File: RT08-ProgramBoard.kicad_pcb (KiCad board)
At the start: 2 copper layers, 325 parts, among them J1 PWR/Addr, J2 Inst-1, J3 Inst-2, J4 Data-1, J5 Data-2

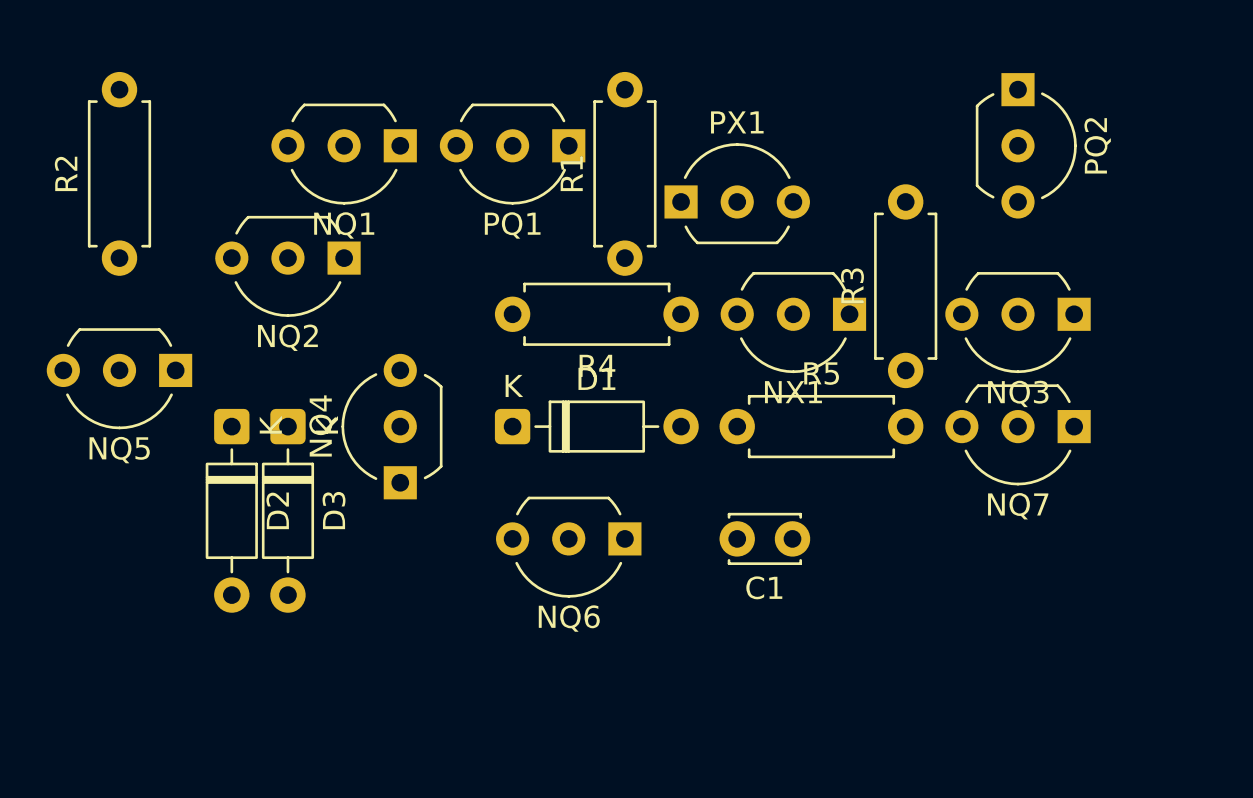
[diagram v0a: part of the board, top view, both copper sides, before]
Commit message: Designing new register circuit
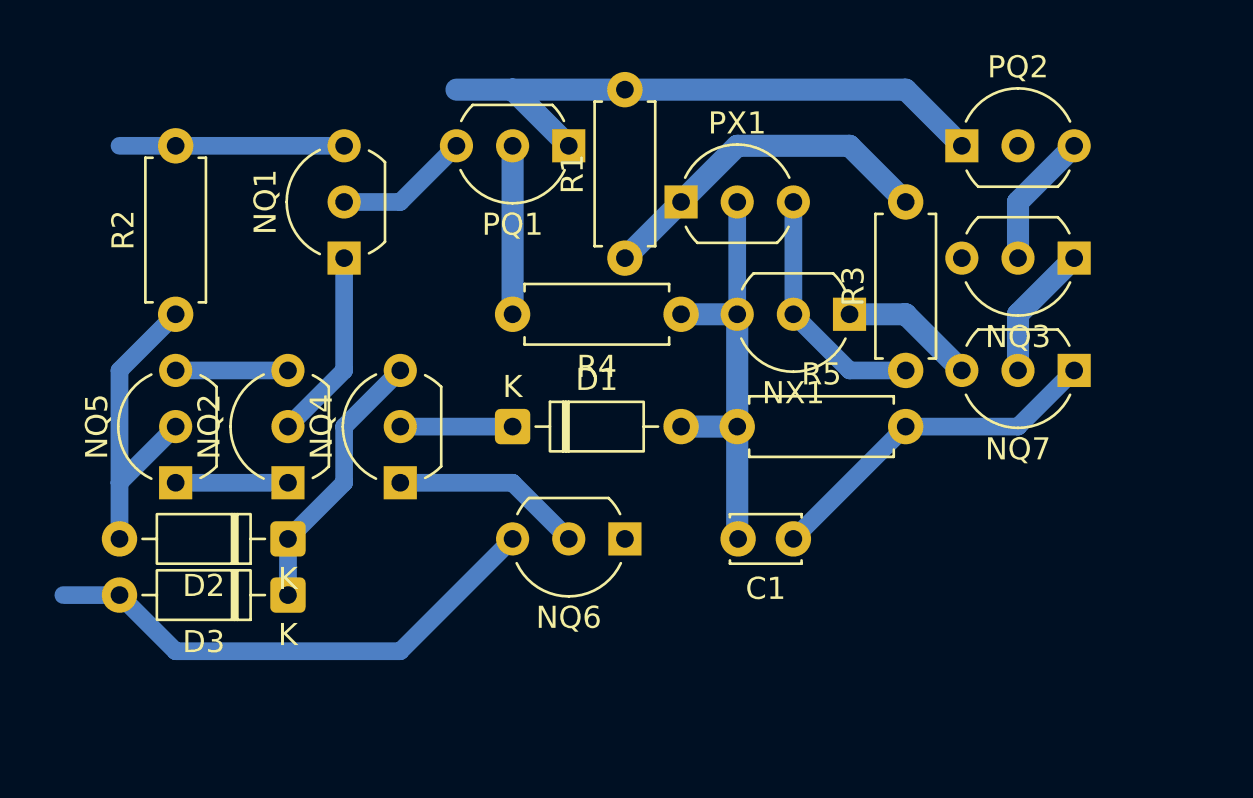
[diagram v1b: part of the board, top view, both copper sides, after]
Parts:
- moved NQ2 10.5 mm to (71.1, 45.7), turned to 90 degrees
- moved D3 7.62 mm to (71.1, 50.8), turned to 180 degrees
- moved NQ1 5.68 mm to (73.7, 35.6), turned to 90 degrees
- moved D2 5.68 mm to (71.1, 48.3), turned to 180 degrees
- moved NQ5 5.08 mm to (66.0, 45.7), turned to 90 degrees
- moved PQ2 3.59 mm to (101.6, 30.5), turned to 0 degrees
- moved R2 3.59 mm to (66.0, 38.1)
- moved NQ3 2.54 mm to (106.7, 35.6)
- moved NQ7 2.54 mm to (106.7, 40.6)
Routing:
- net +5V: track 0.00 -> 27.5 mm
- net /Rst: track 0.00 -> 23.5 mm
- net GND: track 0.00 -> 20.9 mm
- net Net-(D1-A): track 0.00 -> 20.3 mm
- net Net-(PX1-E): track 0.00 -> 15.9 mm
- net Net-(D2-A): track 0.00 -> 14.8 mm
- net Net-(D2-K): track 0.00 -> 12.3 mm
- net Net-(NX1-C): track 0.00 -> 11.2 mm
- net /WEn: track 0.00 -> 10.2 mm
- net Net-(NQ4-E): track 0.00 -> 8.67 mm
- net Net-(NQ1-E): track 0.00 -> 8.67 mm
- net Net-(PQ1-C): track 0.00 -> 7.62 mm
- net Net-(NQ3-C): track 0.00 -> 6.13 mm
- net Net-(NQ3-E): track 0.00 -> 6.13 mm
- net Net-(NQ1-C): track 0.00 -> 6.13 mm
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
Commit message: New design completed
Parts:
- removed D33, D34, D35, D36, D37, D38, D39, D40, D41, D42, D43, D44, D45, D46, D47, D48: 30V0.2A, Diode_THT:D_DO-35_SOD27_P7.62mm_Horizontal
- removed NQ100, NQ101, NQ103, NQ105, NQ106, NQ107, NQ108, NQ110, NQ112, NQ98, NQ99: DTC114E-THT, Package_TO_SOT_THT:TO-92_Inline_Wide
- removed NQ102, NQ104, NQ109, NQ111, NQ97: DTC143E-THT, Package_TO_SOT_THT:TO-92_Inline_Wide
- J1: value PWR/Addr -> PWR/Ctrl
- NQ10, NQ16, NQ22, NQ28, NQ40, NQ52, NQ58, NQ64, NQ70, NQ82, NQ94: value DTC114E-THT -> DTC143E-THT
- NQ11, NQ13, NQ18, NQ20, NQ25, NQ27, NQ32, NQ39, NQ41, NQ48, NQ53, NQ55, NQ6, NQ60, NQ62, NQ67, NQ69, NQ74, NQ81, NQ83, NQ90, NQ95: value DTC143E-THT -> DTC114E-THT
- moved J1 322.0 mm to (55.9, 137.2), turned to -90 degrees
- moved PQ25 315.1 mm to (53.3, 109.2), turned to 180 degrees
- moved C13 310.3 mm to (55.9, 119.4)
- moved R61 310.1 mm to (38.1, 116.8), turned to 90 degrees
- moved PX13 309.7 mm to (58.4, 111.8)
- moved J2 308.9 mm to (73.7, 137.2), turned to -90 degrees
- moved NQ51 305.3 mm to (40.6, 99.1), turned to 90 degrees
- moved NQ50 297.7 mm to (48.3, 91.4), turned to 180 degrees
- moved NX13 296.4 mm to (66.0, 116.8), turned to 180 degrees
- moved J3 295.7 mm to (91.4, 137.2), turned to -90 degrees
- moved R62 291.6 mm to (55.9, 114.3), turned to 90 degrees
- moved NQ52 290.5 mm to (66.0, 96.5), turned to 180 degrees
- moved R64 288.5 mm to (58.4, 116.8), turned to 180 degrees
- moved NQ27 287.9 mm to (40.6, 71.1), turned to 90 degrees
- moved PQ26 285.8 mm to (71.1, 109.2)
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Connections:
- C1 pad 2: Net-(D1-A) -> Net-(NQ4-C)
- C10 pad 2: Net-(D28-A) -> Net-(NQ58-C)
- C11 pad 2: Net-(D31-A) -> Net-(NQ64-C)
- C12 pad 2: Net-(D34-A) -> Net-(NQ70-C)
- C13 pad 2: Net-(D37-A) -> Net-(NQ76-C)
- C14 pad 2: Net-(D40-A) -> Net-(NQ82-C)
- C15 pad 2: Net-(D43-A) -> Net-(NQ88-C)
- C16 pad 2: Net-(D46-A) -> Net-(NQ94-C)
- C2 pad 2: Net-(D4-A) -> Net-(NQ10-C)
- C3 pad 2: Net-(D7-A) -> Net-(NQ16-C)
- C4 pad 2: Net-(D10-A) -> Net-(NQ22-C)
- C5 pad 2: Net-(D13-A) -> Net-(NQ28-C)
- C6 pad 2: Net-(D16-A) -> Net-(NQ34-C)
- C7 pad 2: Net-(D19-A) -> Net-(NQ40-C)
- C8 pad 2: Net-(D22-A) -> Net-(NQ46-C)
- C9 pad 2: Net-(D25-A) -> Net-(NQ52-C)
- D10 pad 2: Net-(D10-A) -> /Rst
- D14 pad 1: Net-(D14-K) -> Net-(D13-K)
- D14 pad 2: Net-(D14-A) -> /Rst
- D15 pad 1: Net-(D14-K) -> Net-(D15-K)
- D15 pad 2: /Rst -> Net-(D15-A)
- D16 pad 1: Net-(D16-K) -> Net-(D15-K)
- D16 pad 2: Net-(D16-A) -> /Rst
- D2 pad 1: Net-(D2-K) -> Net-(D1-K)
- D2 pad 2: Net-(D2-A) -> /Rst
- D20 pad 1: Net-(D20-K) -> Net-(D19-K)
- D20 pad 2: Net-(D20-A) -> /Rst
- D21 pad 1: Net-(D20-K) -> Net-(D21-K)
- D21 pad 2: /Rst -> Net-(D21-A)
- D22 pad 1: Net-(D22-K) -> Net-(D21-K)
- D22 pad 2: Net-(D22-A) -> /Rst
- D26 pad 1: Net-(D26-K) -> Net-(D25-K)
- D26 pad 2: Net-(D26-A) -> /Rst
- D27 pad 1: Net-(D26-K) -> Net-(D27-K)
- D27 pad 2: /Rst -> Net-(D27-A)
- D28 pad 1: Net-(D28-K) -> Net-(D27-K)
- D28 pad 2: Net-(D28-A) -> /Rst
- D3 pad 1: Net-(D2-K) -> Net-(D3-K)
- D3 pad 2: /Rst -> Net-(D3-A)
- D32 pad 1: Net-(D32-K) -> Net-(D31-K)
- D32 pad 2: Net-(D32-A) -> /Rst
- D4 pad 1: Net-(D4-K) -> Net-(D3-K)
- D4 pad 2: Net-(D4-A) -> /Rst
- D8 pad 1: Net-(D8-K) -> Net-(D7-K)
- D8 pad 2: Net-(D8-A) -> /Rst
- D9 pad 1: Net-(D8-K) -> Net-(D10-K)
- D9 pad 2: /Rst -> Net-(D9-A)
- J1 pad 2: /WEn -> /DEn
- J1 pad 3: /DEn -> /WEn
- NQ10 pad 1: Net-(NQ10-E) -> GND
- NQ10 pad 3: /DEn -> Net-(D3-K)
- NQ11 pad 2: Net-(D4-K) -> Net-(NQ11-C)
- NQ11 pad 3: Net-(D5-K) -> /DEn
- NQ12 pad 2: Net-(D5-A) -> Net-(NQ11-E)
- NQ12 pad 3: /D1 -> Net-(NQ12-B)
- NQ13 pad 1: GND -> Net-(NQ13-E)
- NQ13 pad 2: Net-(NQ11-E) -> Net-(NQ13-C)
- NQ13 pad 3: /Rst -> /WEn
- NQ14 pad 2: Net-(NQ10-E) -> Net-(NQ13-E)
- NQ14 pad 3: Net-(NQ14-B) -> /D2
- NQ15 pad 1: Net-(NQ15-E) -> GND
- NQ15 pad 2: Net-(NQ15-C) -> Net-(D5-A)
- NQ15 pad 3: /WEn -> /D2
- NQ16 pad 2: Net-(NQ15-E) -> Net-(NQ16-C)
- NQ16 pad 3: /D2 -> Net-(D5-K)
- NQ18 pad 1: Net-(NQ18-E) -> GND
- NQ18 pad 2: Net-(D7-K) -> Net-(NQ17-E)
- NQ18 pad 3: Net-(D8-K) -> Net-(NQ18-B)
- NQ19 pad 1: GND -> Net-(NQ19-E)
- NQ19 pad 2: Net-(D8-A) -> Net-(NQ19-C)
- NQ19 pad 3: /D2 -> /WEn
- NQ20 pad 2: Net-(NQ18-E) -> Net-(NQ19-E)
- NQ20 pad 3: /Rst -> /D3
- NQ21 pad 2: Net-(NQ17-E) -> Net-(D7-A)
- NQ21 pad 3: Net-(NQ21-B) -> /D3
- NQ22 pad 1: Net-(NQ22-E) -> GND
- NQ22 pad 3: /WEn -> Net-(D7-K)
- NQ23 pad 1: GND -> Net-(NQ23-E)
- NQ23 pad 2: Net-(NQ22-E) -> Net-(NQ23-C)
- NQ23 pad 3: /D3 -> /DEn
- NQ24 pad 1: Net-(NQ24-E) -> GND
- NQ24 pad 2: Net-(NQ24-C) -> Net-(NQ23-E)
- NQ24 pad 3: /DEn -> Net-(NQ24-B)
- NQ25 pad 2: Net-(D10-K) -> Net-(NQ25-C)
- NQ25 pad 3: Net-(D11-K) -> /WEn
- NQ26 pad 2: Net-(D11-A) -> Net-(NQ25-E)
- NQ26 pad 3: /D3 -> /D4
- NQ27 pad 2: Net-(NQ25-E) -> Net-(D9-A)
- NQ27 pad 3: /Rst -> /D4
- NQ28 pad 2: Net-(NQ24-E) -> Net-(NQ28-C)
- NQ28 pad 3: Net-(NQ28-B) -> Net-(D10-K)
- NQ29 pad 3: /WEn -> /DEn
- NQ3 pad 1: Net-(NQ3-E) -> GND
- NQ3 pad 2: Net-(NQ3-C) -> Net-(D1-A)
- NQ3 pad 3: /DEn -> /D0
- NQ30 pad 3: /D4 -> Net-(NQ30-B)
- NQ31 pad 3: /DEn -> /WEn
- NQ32 pad 1: Net-(NQ32-E) -> GND
- NQ32 pad 2: Net-(D13-K) -> Net-(NQ31-E)
- NQ32 pad 3: Net-(D14-K) -> /D5
- NQ33 pad 2: Net-(D14-A) -> Net-(D11-A)
- NQ33 pad 3: /D4 -> /D5
- NQ34 pad 2: Net-(NQ32-E) -> Net-(NQ34-C)
- NQ34 pad 3: /Rst -> Net-(D11-K)
- NQ35 pad 1: GND -> Net-(NQ35-E)
- NQ35 pad 2: Net-(NQ31-E) -> Net-(NQ35-C)
- NQ35 pad 3: Net-(NQ35-B) -> /DEn
- NQ36 pad 1: Net-(NQ36-E) -> GND
- NQ36 pad 2: Net-(NQ36-C) -> Net-(NQ35-E)
- NQ36 pad 3: /WEn -> Net-(NQ36-B)
- NQ37 pad 1: GND -> Net-(NQ37-E)
- NQ37 pad 2: Net-(NQ36-E) -> Net-(NQ37-C)
- NQ37 pad 3: /D5 -> /WEn
- NQ38 pad 1: Net-(NQ38-E) -> GND
- NQ38 pad 2: Net-(NQ38-C) -> Net-(NQ37-E)
- NQ38 pad 3: /DEn -> /D6
- NQ39 pad 1: Net-(NQ39-E) -> GND
- NQ39 pad 2: Net-(D16-K) -> Net-(D13-A)
- NQ39 pad 3: Net-(D17-K) -> /D6
- NQ4 pad 1: Net-(NQ4-E) -> GND
- NQ4 pad 2: Net-(D1-K) -> Net-(NQ4-C)
- NQ4 pad 3: Net-(D2-K) -> Net-(D1-K)
- NQ40 pad 2: Net-(D17-A) -> Net-(NQ40-C)
- NQ40 pad 3: /D5 -> Net-(D13-K)
- NQ41 pad 1: GND -> Net-(NQ41-E)
- NQ41 pad 2: Net-(NQ39-E) -> Net-(NQ41-C)
- NQ41 pad 3: /Rst -> /DEn
- NQ42 pad 2: Net-(NQ38-E) -> Net-(NQ41-E)
- NQ44 pad 3: /D6 -> /D7
- NQ45 pad 1: Net-(NQ45-E) -> GND
- NQ45 pad 2: Net-(NQ45-C) -> Net-(D15-A)
- NQ45 pad 3: /DEn -> /D7
- NQ46 pad 1: Net-(NQ46-E) -> GND
- NQ46 pad 2: Net-(D19-K) -> Net-(NQ46-C)
- NQ46 pad 3: Net-(D20-K) -> Net-(D15-K)
- NQ47 pad 1: GND -> Net-(NQ47-E)
- NQ47 pad 2: Net-(D20-A) -> Net-(NQ47-C)
- NQ47 pad 3: /D6 -> /DEn
- NQ48 pad 2: Net-(NQ46-E) -> Net-(NQ47-E)
- NQ48 pad 3: /Rst -> Net-(NQ48-B)
- NQ49 pad 1: GND -> Net-(NQ49-E)
- NQ49 pad 2: Net-(NQ45-E) -> Net-(NQ49-C)
- NQ49 pad 3: Net-(NQ49-B) -> /WEn
- NQ5 pad 1: GND -> Net-(NQ5-E)
- NQ5 pad 2: Net-(D2-A) -> Net-(NQ5-C)
- NQ5 pad 3: /D0 -> /DEn
- NQ50 pad 1: Net-(NQ50-E) -> GND
- NQ50 pad 2: Net-(NQ50-C) -> Net-(NQ49-E)
- NQ50 pad 3: /WEn -> /D8
- NQ51 pad 2: Net-(NQ50-E) -> Net-(D17-A)
- NQ51 pad 3: /D7 -> /D8
- NQ52 pad 1: Net-(NQ52-E) -> GND
- NQ52 pad 3: /DEn -> Net-(D17-K)
- NQ53 pad 2: Net-(D22-K) -> Net-(NQ53-C)
- NQ53 pad 3: Net-(D23-K) -> /DEn
- NQ54 pad 2: Net-(D23-A) -> Net-(NQ53-E)
- NQ54 pad 3: /D7 -> Net-(NQ54-B)
- NQ55 pad 1: GND -> Net-(NQ55-E)
- NQ55 pad 2: Net-(NQ53-E) -> Net-(NQ55-C)
- NQ55 pad 3: /Rst -> /WEn
- NQ56 pad 2: Net-(NQ52-E) -> Net-(NQ55-E)
- NQ56 pad 3: Net-(NQ56-B) -> /D9
- NQ57 pad 1: Net-(NQ57-E) -> GND
- NQ57 pad 2: Net-(NQ57-C) -> Net-(D19-A)
- NQ57 pad 3: /WEn -> /D9
- NQ58 pad 2: Net-(NQ57-E) -> Net-(NQ58-C)
- NQ58 pad 3: /D8 -> Net-(D19-K)
- NQ6 pad 2: Net-(NQ4-E) -> Net-(NQ5-E)
- NQ6 pad 3: /Rst -> Net-(NQ6-B)
- NQ60 pad 1: Net-(NQ60-E) -> GND
- NQ60 pad 2: Net-(D25-K) -> Net-(NQ59-E)
- NQ60 pad 3: Net-(D26-K) -> Net-(NQ60-B)
- NQ61 pad 1: GND -> Net-(NQ61-E)
- NQ61 pad 2: Net-(D26-A) -> Net-(NQ61-C)
- NQ61 pad 3: /D8 -> /WEn
- NQ62 pad 2: Net-(NQ60-E) -> Net-(NQ61-E)
- NQ62 pad 3: /Rst -> /D10
- NQ63 pad 2: Net-(NQ59-E) -> Net-(D21-A)
- NQ63 pad 3: Net-(NQ63-B) -> /D10
- NQ64 pad 1: Net-(NQ64-E) -> GND
- NQ64 pad 3: /WEn -> Net-(D21-K)
- NQ65 pad 1: GND -> Net-(NQ65-E)
- NQ65 pad 2: Net-(NQ64-E) -> Net-(NQ65-C)
- NQ65 pad 3: /D9 -> /DEn
- NQ66 pad 1: Net-(NQ66-E) -> GND
- NQ66 pad 2: Net-(NQ66-C) -> Net-(NQ65-E)
- NQ66 pad 3: /DEn -> Net-(NQ66-B)
- NQ67 pad 2: Net-(D28-K) -> Net-(NQ67-C)
- NQ67 pad 3: Net-(D29-K) -> /WEn
- NQ68 pad 2: Net-(D29-A) -> Net-(NQ67-E)
- NQ68 pad 3: /D9 -> /D11
- NQ69 pad 2: Net-(NQ67-E) -> Net-(D23-A)
- NQ69 pad 3: /Rst -> /D11
- NQ7 pad 1: GND -> Net-(NQ7-E)
- NQ7 pad 2: Net-(NQ3-E) -> Net-(NQ7-C)
- NQ7 pad 3: Net-(NQ7-B) -> /WEn
- NQ70 pad 2: Net-(NQ66-E) -> Net-(NQ70-C)
- NQ70 pad 3: Net-(NQ70-B) -> Net-(D23-K)
- NQ71 pad 3: /WEn -> /DEn
- NQ72 pad 3: /D10 -> Net-(NQ72-B)
- NQ73 pad 3: /DEn -> /WEn
- NQ74 pad 1: Net-(NQ74-E) -> GND
- NQ74 pad 2: Net-(D31-K) -> Net-(NQ73-E)
- NQ74 pad 3: Net-(D32-K) -> /D12
- NQ75 pad 2: Net-(D32-A) -> Net-(D25-A)
- NQ75 pad 3: /D10 -> /D12
- NQ76 pad 2: Net-(NQ74-E) -> Net-(NQ76-C)
- NQ76 pad 3: /Rst -> Net-(D25-K)
- NQ77 pad 1: GND -> Net-(NQ77-E)
- NQ77 pad 2: Net-(NQ73-E) -> Net-(NQ77-C)
- NQ77 pad 3: Net-(NQ77-B) -> /DEn
- NQ78 pad 1: Net-(NQ78-E) -> GND
- NQ78 pad 2: Net-(NQ78-C) -> Net-(NQ77-E)
- NQ78 pad 3: /WEn -> Net-(NQ78-B)
- NQ79 pad 1: GND -> Net-(NQ79-E)
- NQ79 pad 2: Net-(NQ78-E) -> Net-(NQ79-C)
- NQ79 pad 3: /D11 -> /WEn
- NQ8 pad 1: Net-(NQ8-E) -> GND
- NQ8 pad 2: Net-(NQ8-C) -> Net-(NQ7-E)
- NQ8 pad 3: /WEn -> /D1
- NQ80 pad 1: Net-(NQ80-E) -> GND
- NQ80 pad 2: Net-(NQ80-C) -> Net-(NQ79-E)
- NQ80 pad 3: /DEn -> /D13
- NQ81 pad 1: Net-(NQ81-E) -> GND
- NQ81 pad 2: Net-(D34-K) -> Net-(D27-A)
- NQ81 pad 3: Net-(D35-K) -> /D13
- NQ82 pad 2: Net-(D35-A) -> Net-(NQ82-C)
- NQ82 pad 3: /D11 -> Net-(D27-K)
- NQ83 pad 1: GND -> Net-(NQ83-E)
- NQ83 pad 2: Net-(NQ81-E) -> Net-(NQ83-C)
- NQ83 pad 3: /Rst -> /DEn
- NQ84 pad 2: Net-(NQ80-E) -> Net-(NQ83-E)
- NQ86 pad 3: /D12 -> /D14
- NQ87 pad 1: Net-(NQ87-E) -> GND
- NQ87 pad 2: Net-(NQ87-C) -> Net-(D29-A)
- NQ87 pad 3: /DEn -> /D14
- NQ88 pad 1: Net-(NQ88-E) -> GND
- NQ88 pad 2: Net-(D37-K) -> Net-(NQ88-C)
- NQ88 pad 3: Net-(D38-K) -> Net-(D29-K)
- NQ89 pad 1: GND -> Net-(NQ89-E)
- NQ89 pad 2: Net-(D38-A) -> Net-(NQ89-C)
- NQ89 pad 3: /D12 -> /DEn
- NQ9 pad 2: Net-(NQ8-E) -> Net-(D3-A)
- NQ90 pad 2: Net-(NQ88-E) -> Net-(NQ89-E)
- NQ90 pad 3: /Rst -> Net-(NQ90-B)
- NQ91 pad 1: GND -> Net-(NQ91-E)
- NQ91 pad 2: Net-(NQ87-E) -> Net-(NQ91-C)
- NQ91 pad 3: Net-(NQ91-B) -> /WEn
- NQ92 pad 1: Net-(NQ92-E) -> GND
- NQ92 pad 2: Net-(NQ92-C) -> Net-(NQ91-E)
- NQ92 pad 3: /WEn -> /D15
- NQ93 pad 2: Net-(NQ92-E) -> Net-(D31-A)
- NQ93 pad 3: /D13 -> /D15
- NQ94 pad 1: Net-(NQ94-E) -> GND
- NQ94 pad 3: /DEn -> Net-(D31-K)
- NQ95 pad 2: Net-(D40-K) -> Net-(NQ95-C)
- NQ95 pad 3: Net-(D41-K) -> /DEn
- NQ96 pad 2: Net-(D41-A) -> Net-(NQ95-E)
- NQ96 pad 3: /D13 -> Net-(NQ96-B)
- NX1 pad 1: Net-(NQ7-B) -> Net-(NQ6-B)
- NX1 pad 3: Net-(D1-A) -> Net-(NQ4-C)
- NX10 pad 1: Net-(NQ70-B) -> Net-(NQ60-B)
- NX10 pad 3: Net-(D28-A) -> Net-(NQ58-C)
- NX11 pad 1: Net-(NQ77-B) -> Net-(NQ66-B)
- NX11 pad 3: Net-(D31-A) -> Net-(NQ64-C)
- NX12 pad 1: Net-(NQ84-B) -> Net-(NQ72-B)
- NX12 pad 3: Net-(D34-A) -> Net-(NQ70-C)
- NX13 pad 1: Net-(NQ91-B) -> Net-(NQ78-B)
- NX13 pad 3: Net-(D37-A) -> Net-(NQ76-C)
- NX14 pad 1: Net-(NQ98-B) -> Net-(NQ84-B)
- NX14 pad 3: Net-(D40-A) -> Net-(NQ82-C)
- NX15 pad 1: Net-(NQ105-B) -> Net-(NQ90-B)
- NX15 pad 3: Net-(D43-A) -> Net-(NQ88-C)
- NX16 pad 1: Net-(NQ112-B) -> Net-(NQ96-B)
- NX16 pad 3: Net-(D46-A) -> Net-(NQ94-C)
- NX2 pad 1: Net-(NQ14-B) -> Net-(NQ12-B)
- NX2 pad 3: Net-(D4-A) -> Net-(NQ10-C)
- NX3 pad 1: Net-(NQ21-B) -> Net-(NQ18-B)
- NX3 pad 3: Net-(D7-A) -> Net-(NQ16-C)
- NX4 pad 1: Net-(NQ28-B) -> Net-(NQ24-B)
- NX4 pad 3: Net-(D10-A) -> Net-(NQ22-C)
- NX5 pad 1: Net-(NQ35-B) -> Net-(NQ30-B)
- NX5 pad 3: Net-(D13-A) -> Net-(NQ28-C)
- NX6 pad 1: Net-(NQ42-B) -> Net-(NQ36-B)
- NX6 pad 3: Net-(D16-A) -> Net-(NQ34-C)
- NX7 pad 1: Net-(NQ49-B) -> Net-(NQ42-B)
- NX7 pad 3: Net-(D19-A) -> Net-(NQ40-C)
- NX8 pad 1: Net-(NQ56-B) -> Net-(NQ48-B)
- NX8 pad 3: Net-(D22-A) -> Net-(NQ46-C)
- NX9 pad 1: Net-(NQ63-B) -> Net-(NQ54-B)
- NX9 pad 3: Net-(D25-A) -> Net-(NQ52-C)
- PQ10 pad 3: Net-(NQ31-C) -> Net-(NQ29-C)
- PQ11 pad 3: Net-(NQ36-C) -> Net-(NQ31-C)
- PQ12 pad 3: Net-(NQ38-C) -> Net-(NQ35-C)
- PQ13 pad 3: Net-(NQ43-C) -> Net-(NQ37-C)
- PQ14 pad 3: Net-(NQ45-C) -> Net-(NQ41-C)
- PQ15 pad 3: Net-(NQ50-C) -> Net-(NQ43-C)
- PQ16 pad 3: Net-(NQ52-C) -> Net-(NQ47-C)
- PQ17 pad 3: Net-(NQ57-C) -> Net-(NQ49-C)
- PQ18 pad 3: Net-(NQ59-C) -> Net-(NQ53-C)
- PQ19 pad 3: Net-(NQ64-C) -> Net-(NQ55-C)
- PQ2 pad 3: Net-(NQ3-C) -> Net-(NQ5-C)
- PQ20 pad 3: Net-(NQ66-C) -> Net-(NQ59-C)
- PQ21 pad 3: Net-(NQ71-C) -> Net-(NQ61-C)
- PQ22 pad 3: Net-(NQ73-C) -> Net-(NQ65-C)
- PQ23 pad 3: Net-(NQ78-C) -> Net-(NQ67-C)
- PQ24 pad 3: Net-(NQ80-C) -> Net-(NQ71-C)
- PQ25 pad 3: Net-(NQ85-C) -> Net-(NQ73-C)
- PQ26 pad 3: Net-(NQ87-C) -> Net-(NQ77-C)
- PQ27 pad 3: Net-(NQ92-C) -> Net-(NQ79-C)
- PQ28 pad 3: Net-(NQ94-C) -> Net-(NQ83-C)
- PQ29 pad 3: Net-(NQ99-C) -> Net-(NQ85-C)
- PQ3 pad 3: Net-(NQ8-C) -> Net-(NQ7-C)
- PQ30 pad 3: Net-(NQ101-C) -> Net-(NQ89-C)
- PQ31 pad 3: Net-(NQ106-C) -> Net-(NQ91-C)
- PQ32 pad 3: Net-(NQ108-C) -> Net-(NQ95-C)
- PQ4 pad 3: Net-(NQ10-C) -> Net-(NQ11-C)
- PQ5 pad 3: Net-(NQ15-C) -> Net-(NQ13-C)
- PQ7 pad 3: Net-(NQ22-C) -> Net-(NQ19-C)
- PQ8 pad 3: Net-(NQ24-C) -> Net-(NQ23-C)
- PQ9 pad 3: Net-(NQ29-C) -> Net-(NQ25-C)
- PX1 pad 2: Net-(D1-A) -> Net-(NQ4-C)
- PX10 pad 2: Net-(D28-A) -> Net-(NQ58-C)
- PX11 pad 2: Net-(D31-A) -> Net-(NQ64-C)
- PX12 pad 2: Net-(D34-A) -> Net-(NQ70-C)
- PX13 pad 2: Net-(D37-A) -> Net-(NQ76-C)
- PX14 pad 2: Net-(D40-A) -> Net-(NQ82-C)
- PX15 pad 2: Net-(D43-A) -> Net-(NQ88-C)
- PX16 pad 2: Net-(D46-A) -> Net-(NQ94-C)
- PX2 pad 2: Net-(D4-A) -> Net-(NQ10-C)
- PX3 pad 2: Net-(D7-A) -> Net-(NQ16-C)
- PX4 pad 2: Net-(D10-A) -> Net-(NQ22-C)
- PX5 pad 2: Net-(D13-A) -> Net-(NQ28-C)
- PX6 pad 2: Net-(D16-A) -> Net-(NQ34-C)
- PX7 pad 2: Net-(D19-A) -> Net-(NQ40-C)
- PX8 pad 2: Net-(D22-A) -> Net-(NQ46-C)
- PX9 pad 2: Net-(D25-A) -> Net-(NQ52-C)
- R1 pad 1: Net-(PX1-E) -> Net-(D1-A)
- R1 pad 2: +5V -> /WEn
- R10 pad 1: Net-(D4-A) -> Net-(NQ10-C)
- R11 pad 1: Net-(PX3-E) -> Net-(D5-A)
- R11 pad 2: +5V -> /WEn
- R12 pad 1: Net-(D8-A) -> Net-(PX3-E)
- R12 pad 2: /WEn -> +5V
- R14 pad 1: Net-(D7-A) -> Net-(NQ16-C)
- R15 pad 1: Net-(D7-A) -> Net-(NQ16-C)
- R16 pad 1: Net-(PX4-E) -> Net-(D7-A)
- R16 pad 2: +5V -> /WEn
- R17 pad 1: Net-(D11-A) -> Net-(PX4-E)
- R17 pad 2: /WEn -> +5V
- R19 pad 1: Net-(D10-A) -> Net-(NQ22-C)
- R2 pad 1: Net-(D2-A) -> Net-(PX1-E)
- R2 pad 2: /WEn -> +5V
- R20 pad 1: Net-(D10-A) -> Net-(NQ22-C)
- R21 pad 1: Net-(PX5-E) -> Net-(D9-A)
- R21 pad 2: +5V -> /WEn
- R22 pad 1: Net-(D14-A) -> Net-(PX5-E)
- R22 pad 2: /WEn -> +5V
- R24 pad 1: Net-(D13-A) -> Net-(NQ28-C)
- R25 pad 1: Net-(D13-A) -> Net-(NQ28-C)
- R26 pad 1: Net-(PX6-E) -> Net-(D11-A)
- R26 pad 2: +5V -> /WEn
- R27 pad 1: Net-(D17-A) -> Net-(PX6-E)
- R27 pad 2: /WEn -> +5V
- R29 pad 1: Net-(D16-A) -> Net-(NQ34-C)
- R30 pad 1: Net-(D16-A) -> Net-(NQ34-C)
- R31 pad 1: Net-(PX7-E) -> Net-(D13-A)
- R31 pad 2: +5V -> /WEn
- R32 pad 1: Net-(D20-A) -> Net-(PX7-E)
- R32 pad 2: /WEn -> +5V
- R34 pad 1: Net-(D19-A) -> Net-(NQ40-C)
- R35 pad 1: Net-(D19-A) -> Net-(NQ40-C)
- R36 pad 1: Net-(PX8-E) -> Net-(D15-A)
- R36 pad 2: +5V -> /WEn
- R37 pad 1: Net-(D23-A) -> Net-(PX8-E)
- R37 pad 2: /WEn -> +5V
- R39 pad 1: Net-(D22-A) -> Net-(NQ46-C)
- R4 pad 1: Net-(D1-A) -> Net-(NQ4-C)
- R40 pad 1: Net-(D22-A) -> Net-(NQ46-C)
- R41 pad 1: Net-(PX9-E) -> Net-(D17-A)
- R41 pad 2: +5V -> /WEn
- R42 pad 1: Net-(D26-A) -> Net-(PX9-E)
- R42 pad 2: /WEn -> +5V
- R44 pad 1: Net-(D25-A) -> Net-(NQ52-C)
- R45 pad 1: Net-(D25-A) -> Net-(NQ52-C)
- R46 pad 1: Net-(PX10-E) -> Net-(D19-A)
- R46 pad 2: +5V -> /WEn
- R47 pad 1: Net-(D29-A) -> Net-(PX10-E)
- R47 pad 2: /WEn -> +5V
- R49 pad 1: Net-(D28-A) -> Net-(NQ58-C)
- R5 pad 1: Net-(D1-A) -> Net-(NQ4-C)
- R50 pad 1: Net-(D28-A) -> Net-(NQ58-C)
- R51 pad 1: Net-(PX11-E) -> Net-(D21-A)
- R51 pad 2: +5V -> /WEn
- R52 pad 1: Net-(D32-A) -> Net-(PX11-E)
- R52 pad 2: /WEn -> +5V
- R54 pad 1: Net-(D31-A) -> Net-(NQ64-C)
- R55 pad 1: Net-(D31-A) -> Net-(NQ64-C)
- R56 pad 1: Net-(PX12-E) -> Net-(D23-A)
- R56 pad 2: +5V -> /WEn
- R57 pad 1: Net-(D35-A) -> Net-(PX12-E)
- R57 pad 2: /WEn -> +5V
- R59 pad 1: Net-(D34-A) -> Net-(NQ70-C)
- R6 pad 1: Net-(PX2-E) -> Net-(D3-A)
- R6 pad 2: +5V -> /WEn
- R60 pad 1: Net-(D34-A) -> Net-(NQ70-C)
- R61 pad 1: Net-(PX13-E) -> Net-(D25-A)
- R61 pad 2: +5V -> /WEn
- R62 pad 1: Net-(D38-A) -> Net-(PX13-E)
- R62 pad 2: /WEn -> +5V
- R64 pad 1: Net-(D37-A) -> Net-(NQ76-C)
- R65 pad 1: Net-(D37-A) -> Net-(NQ76-C)
- R66 pad 1: Net-(PX14-E) -> Net-(D27-A)
- R66 pad 2: +5V -> /WEn
- R67 pad 1: Net-(D41-A) -> Net-(PX14-E)
- R67 pad 2: /WEn -> +5V
- R69 pad 1: Net-(D40-A) -> Net-(NQ82-C)
- R7 pad 1: Net-(D5-A) -> Net-(PX2-E)
- R7 pad 2: /WEn -> +5V
- R70 pad 1: Net-(D40-A) -> Net-(NQ82-C)
- R71 pad 1: Net-(PX15-E) -> Net-(D29-A)
- R71 pad 2: +5V -> /WEn
- R72 pad 1: Net-(D44-A) -> Net-(PX15-E)
- R72 pad 2: /WEn -> +5V
- R74 pad 1: Net-(D43-A) -> Net-(NQ88-C)
- R75 pad 1: Net-(D43-A) -> Net-(NQ88-C)
- R76 pad 1: Net-(PX16-E) -> Net-(D31-A)
- R76 pad 2: +5V -> /WEn
- R77 pad 1: Net-(D47-A) -> Net-(PX16-E)
- R77 pad 2: /WEn -> +5V
- R79 pad 1: Net-(D46-A) -> Net-(NQ94-C)
- R80 pad 1: Net-(D46-A) -> Net-(NQ94-C)
- R9 pad 1: Net-(D4-A) -> Net-(NQ10-C)
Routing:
- net GND: track 20.9 -> 1423.7 mm, vias 0 -> 5
- net +5V: track 27.5 -> 801.8 mm, vias 0 -> 1
- net /WEn: track 10.2 -> 81.3 mm
- net Net-(NQ70-C): track 0.00 -> 28.2 mm
- net Net-(NQ64-C): track 0.00 -> 28.2 mm
- net Net-(NQ22-C): track 0.00 -> 28.2 mm
- net Net-(NQ16-C): track 0.00 -> 28.2 mm
- net Net-(NQ58-C): track 0.00 -> 28.2 mm
- net Net-(NQ40-C): track 0.00 -> 28.2 mm
- net Net-(NQ46-C): track 0.00 -> 28.2 mm
- net Net-(NQ10-C): track 0.00 -> 28.2 mm
- net Net-(NQ94-C): track 0.00 -> 28.2 mm
- net Net-(NQ34-C): track 0.00 -> 28.2 mm
- net Net-(NQ88-C): track 0.00 -> 28.2 mm
- net Net-(NQ82-C): track 0.00 -> 28.2 mm
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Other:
- board outline added: 190.5 x 124.5 mm
